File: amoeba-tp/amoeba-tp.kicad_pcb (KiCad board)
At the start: 2 copper layers, 172.5 x 126.6 mm, 153 parts

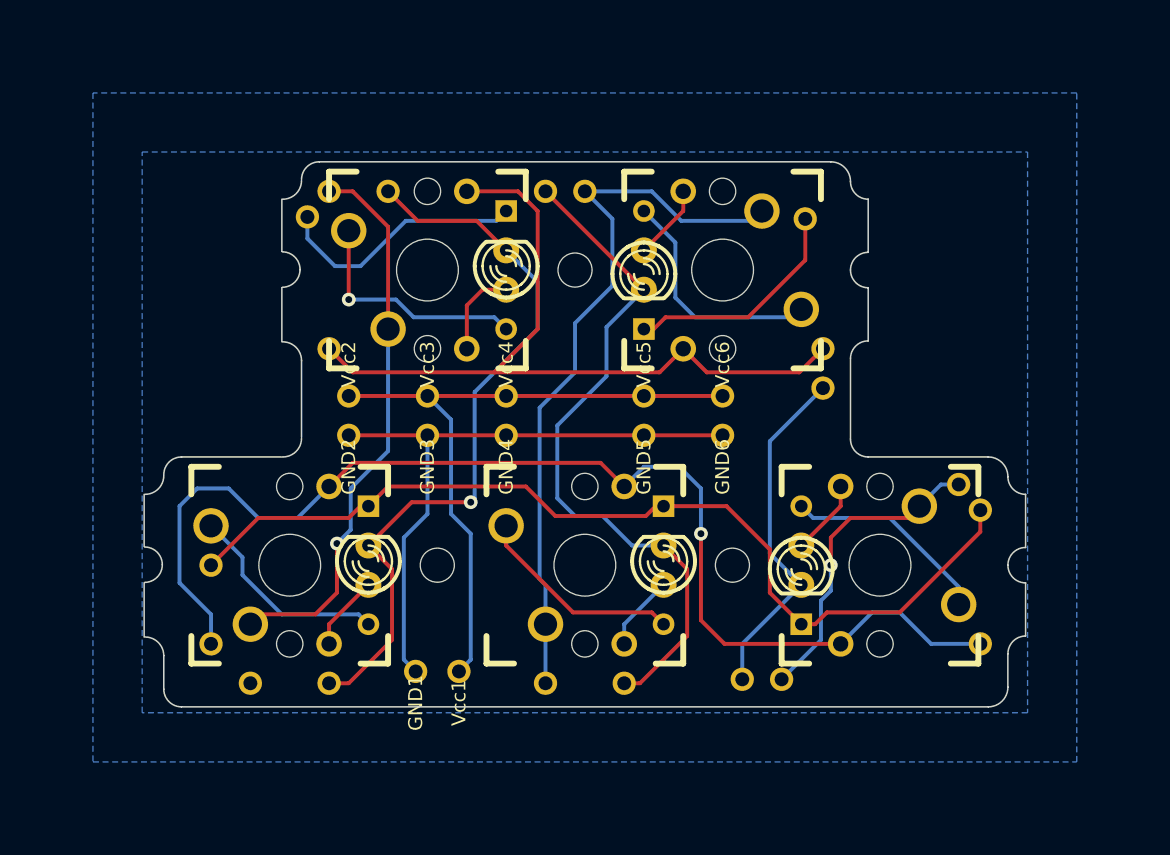
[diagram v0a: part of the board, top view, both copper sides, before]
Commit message: Added fill zones.
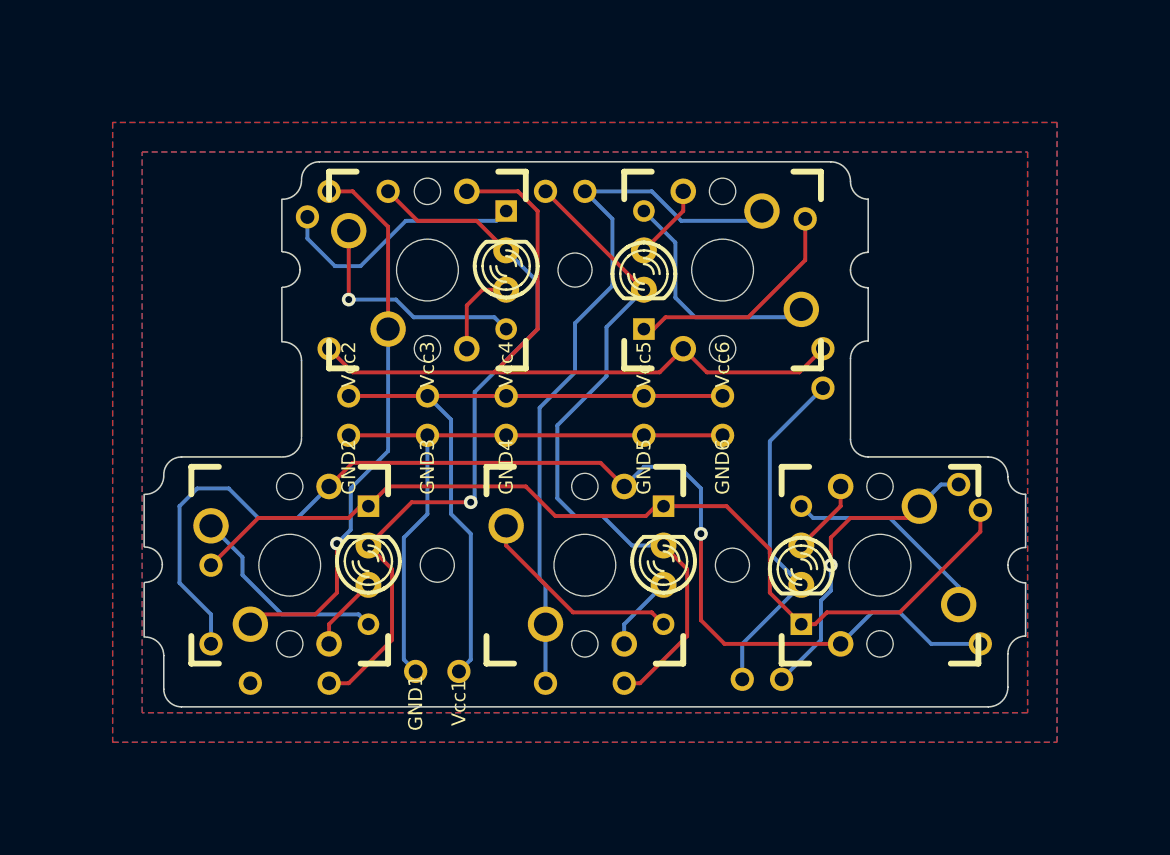
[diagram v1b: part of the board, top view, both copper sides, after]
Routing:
- added copper zone on F.Cu, net N-000007
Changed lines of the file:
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@@
     (links 172)
     (no_connects 40)
-    (area 76.911999 92.024999 172.008001 165.404001)
+    (area 37.184 60.96 220.626 202.846)
     (thickness 1.6)
     (drawings 579)
@@
   (page A3)
   (layers
-    (15 F.Cu signal hide)
+    (15 F.Cu signal)
     (0 B.Cu signal)
     (16 B.Adhes user hide)
@@
     (18 B.Paste user hide)
     (19 F.Paste user hide)
-    (20 B.SilkS user hide)
-    (21 F.SilkS user hide)
+    (20 B.SilkS user)
+    (21 F.SilkS user)
     (22 B.Mask user hide)
     (23 F.Mask user hide)
@@
     (polygon
       (pts
-        (xy 92.71 149.86) (xy 156.21 149.86) (xy 156.21 106.68) (xy 92.71 106.68)
+        (xy 93.98 148.59) (xy 154.94 148.59) (xy 154.94 108.585) (xy 93.98 108.585)
       )
     )
@@
     (polygon
       (pts
-        (xy 95.885 110.49) (xy 95.885 129.54) (xy 95.885 132.08) (xy 96.52 132.08) (xy 97.79 129.54)
-        (xy 104.775 129.54) (xy 105.41 129.54) (xy 106.045 128.905) (xy 106.045 123.825) (xy 104.775 123.19)
-        (xy 104.775 118.745) (xy 105.41 118.745) (xy 105.41 117.475) (xy 104.775 117.475) (xy 104.775 113.03)
-        (xy 105.41 113.03) (xy 106.68 110.49) (xy 104.775 110.49)
+        (xy 106.68 110.49) (xy 105.41 113.03) (xy 104.775 113.03) (xy 104.775 117.475) (xy 105.41 117.475)
+        (xy 105.41 118.745) (xy 104.775 118.745) (xy 104.775 123.19) (xy 106.045 123.825) (xy 106.045 128.905)
+        (xy 105.41 129.54) (xy 97.79 129.54) (xy 96.52 132.08) (xy 95.885 132.08) (xy 95.885 110.49)
+      )
+    )
+  )
+  (zone (net 0) (net_name "") (layer F.Cu) (hatch edge 0.508)
+    (connect_pads (clearance 0.508))
+    (min_thickness 0.254)
+    (keepout (tracks not_allowed) (vias not_allowed) (copperpour not_allowed))
+    (fill (arc_segments 16) (thermal_gap 0.508) (thermal_bridge_width 0.508) (smoothing chamfer))
+    (polygon
+      (pts
+        (xy 163.195 60.96) (xy 164.465 63.5) (xy 165.1 63.5) (xy 165.1 67.945) (xy 164.465 67.945)
+        (xy 164.465 69.215) (xy 165.1 69.215) (xy 165.1 73.66) (xy 163.83 74.295) (xy 163.83 79.375)
+        (xy 164.465 80.01) (xy 172.085 80.01) (xy 173.355 82.55) (xy 173.99 82.55) (xy 173.99 60.96)
+      )
+    )
+  )
+  (zone (net 0) (net_name "") (layer B.Cu) (hatch edge 0.508)
+    (connect_pads (clearance 0.508))
+    (min_thickness 0.254)
+    (keepout (tracks not_allowed) (vias not_allowed) (copperpour not_allowed))
+    (fill (arc_segments 16) (thermal_gap 0.508) (thermal_bridge_width 0.508) (smoothing chamfer))
+    (polygon
+      (pts
+        (xy 140.97 110.49) (xy 142.24 113.03) (xy 142.875 113.03) (xy 142.875 117.475) (xy 142.24 117.475)
+        (xy 142.24 118.745) (xy 142.875 118.745) (xy 142.875 123.19) (xy 141.605 123.825) (xy 141.605 128.905)
+        (xy 142.24 129.54) (xy 151.765 130.175) (xy 152.4 132.08) (xy 153.035 132.08) (xy 153.035 110.49)
+      )
+    )
+  )
+  (zone (net 0) (net_name "") (layer B.Cu) (hatch edge 0.508)
+    (connect_pads (clearance 0.508))
+    (min_thickness 0.254)
+    (keepout (tracks not_allowed) (vias not_allowed) (copperpour not_allowed))
+    (fill (arc_segments 16) (thermal_gap 0.508) (thermal_bridge_width 0.508) (smoothing chamfer))
+    (polygon
+      (pts
+        (xy 153.035 136.525) (xy 152.4 136.525) (xy 152.4 137.795) (xy 153.035 137.795)
+      )
+    )
+  )
+  (zone (net 0) (net_name "") (layer B.Cu) (hatch edge 0.508)
+    (connect_pads (clearance 0.508))
+    (min_thickness 0.254)
+    (keepout (tracks not_allowed) (vias not_allowed) (copperpour not_allowed))
+    (fill (arc_segments 16) (thermal_gap 0.508) (thermal_bridge_width 0.508) (smoothing chamfer))
+    (polygon
+      (pts
+        (xy 153.035 142.24) (xy 152.4 142.24) (xy 152.4 145.415) (xy 151.13 146.685) (xy 153.035 146.685)
+      )
+    )
+  )
+  (zone (net 26) (net_name N-000007) (layer F.Cu) (hatch edge 0.508)
+    (connect_pads (clearance 0.508))
+    (min_thickness 0.254)
+    (fill (arc_segments 16) (thermal_gap 0.508) (thermal_bridge_width 0.508) (smoothing chamfer))
+    (polygon
+      (pts
+        (xy 93.98 148.59) (xy 154.94 148.59) (xy 154.94 108.585) (xy 93.98 108.585)
+      )
+    )
+  )
+  (zone (net 0) (net_name "") (layer F.Cu) (hatch edge 0.508)
+    (priority 1)
+    (connect_pads (clearance 0.508))
+    (min_thickness 0.254)
+    (fill (arc_segments 16) (thermal_gap 0.508) (thermal_bridge_width 0.508) (smoothing chamfer))
+    (polygon
+      (pts
+        (xy 153.035 146.685) (xy 95.885 146.685) (xy 95.885 110.49) (xy 153.035 110.49)
+      )
+    )
+  )
+  (zone (net 0) (net_name "") (layer F.Cu) (hatch edge 0.508)
+    (connect_pads (clearance 0.508))
+    (min_thickness 0.254)
+    (keepout (tracks not_allowed) (vias not_allowed) (copperpour not_allowed))
+    (fill (arc_segments 16) (thermal_gap 0.508) (thermal_bridge_width 0.508) (smoothing chamfer))
+    (polygon
+      (pts
+        (xy 106.68 110.49) (xy 105.41 113.03) (xy 104.775 113.03) (xy 104.775 117.475) (xy 105.41 117.475)
+        (xy 105.41 118.745) (xy 104.775 118.745) (xy 104.775 123.19) (xy 106.045 123.825) (xy 106.045 128.905)
+        (xy 105.41 129.54) (xy 97.79 129.54) (xy 96.52 132.08) (xy 95.885 132.08) (xy 95.885 110.49)
+      )
+    )
+  )
+  (zone (net 0) (net_name "") (layer F.Cu) (hatch edge 0.508)
+    (connect_pads (clearance 0.508))
+    (min_thickness 0.254)
+    (keepout (tracks not_allowed) (vias not_allowed) (copperpour not_allowed))
+    (fill (arc_segments 16) (thermal_gap 0.508) (thermal_bridge_width 0.508) (smoothing chamfer))
+    (polygon
+      (pts
+        (xy 140.97 110.49) (xy 142.24 113.03) (xy 142.875 113.03) (xy 142.875 117.475) (xy 142.24 117.475)
+        (xy 142.24 118.745) (xy 142.875 118.745) (xy 142.875 123.19) (xy 141.605 123.825) (xy 141.605 128.905)
+        (xy 142.24 129.54) (xy 151.765 130.175) (xy 152.4 132.08) (xy 153.035 132.08) (xy 153.035 110.49)
+      )
+    )
+  )
+  (zone (net 0) (net_name "") (layer F.Cu) (hatch edge 0.508)
+    (connect_pads (clearance 0.508))
+    (min_thickness 0.254)
+    (keepout (tracks not_allowed) (vias not_allowed) (copperpour not_allowed))
+    (fill (arc_segments 16) (thermal_gap 0.508) (thermal_bridge_width 0.508) (smoothing chamfer))
+    (polygon
+      (pts
+        (xy 153.035 136.525) (xy 152.4 136.525) (xy 152.4 137.795) (xy 153.035 137.795)
+      )
+    )
+  )
+  (zone (net 0) (net_name "") (layer F.Cu) (hatch edge 0.508)
+    (connect_pads (clearance 0.508))
+    (min_thickness 0.254)
+    (keepout (tracks not_allowed) (vias not_allowed) (copperpour not_allowed))
+    (fill (arc_segments 16) (thermal_gap 0.508) (thermal_bridge_width 0.508) (smoothing chamfer))
+    (polygon
+      (pts
+        (xy 153.035 142.24) (xy 152.4 142.24) (xy 152.4 145.415) (xy 151.13 146.685) (xy 153.035 146.685)
+      )
+    )
+  )
+  (zone (net 0) (net_name "") (layer F.Cu) (hatch edge 0.508)
+    (connect_pads (clearance 0.508))
+    (min_thickness 0.254)
+    (keepout (tracks not_allowed) (vias not_allowed) (copperpour not_allowed))
+    (fill (arc_segments 16) (thermal_gap 0.508) (thermal_bridge_width 0.508) (smoothing chamfer))
+    (polygon
+      (pts
+        (xy 97.79 146.685) (xy 95.885 146.685) (xy 95.885 142.24) (xy 96.52 142.24) (xy 97.155 142.875)
+        (xy 97.155 146.05)
+      )
+    )
+  )
+  (zone (net 0) (net_name "") (layer F.Cu) (hatch edge 0.508)
+    (connect_pads (clearance 0.508))
+    (min_thickness 0.254)
+    (keepout (tracks not_allowed) (vias not_allowed) (copperpour not_allowed))
+    (fill (arc_segments 16) (thermal_gap 0.508) (thermal_bridge_width 0.508) (smoothing chamfer))
+    (polygon
+      (pts
+        (xy 96.52 137.795) (xy 95.885 137.795) (xy 95.885 136.525) (xy 96.52 136.525)
       )
     )

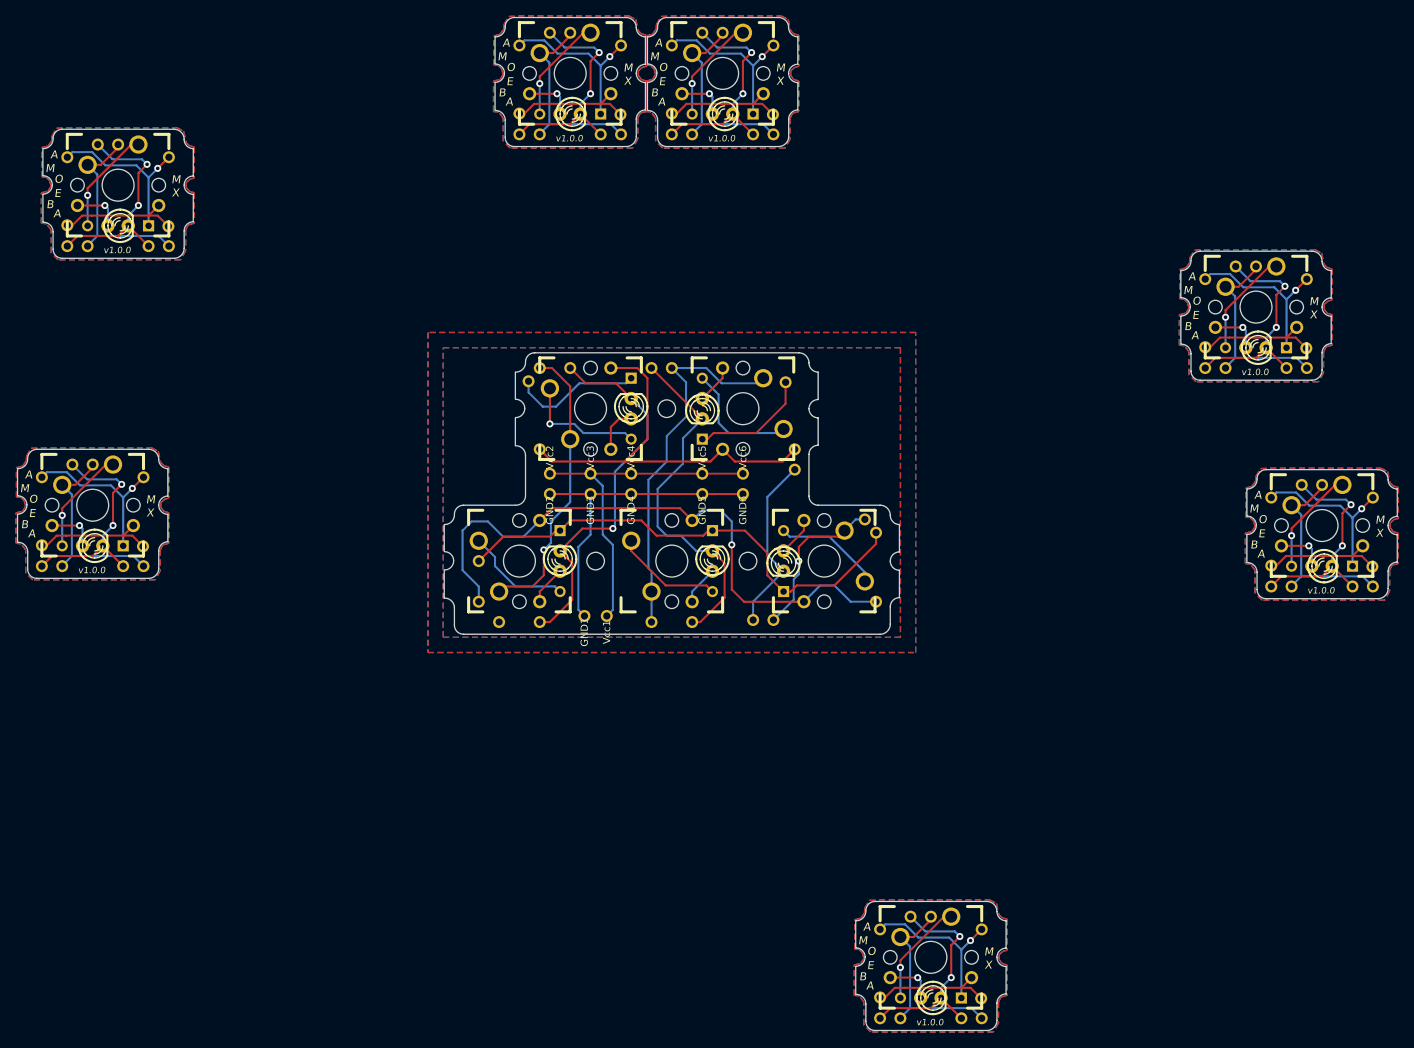
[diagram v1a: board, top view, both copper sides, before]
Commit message: Add labels to PCB and remove Amoeba footprints.
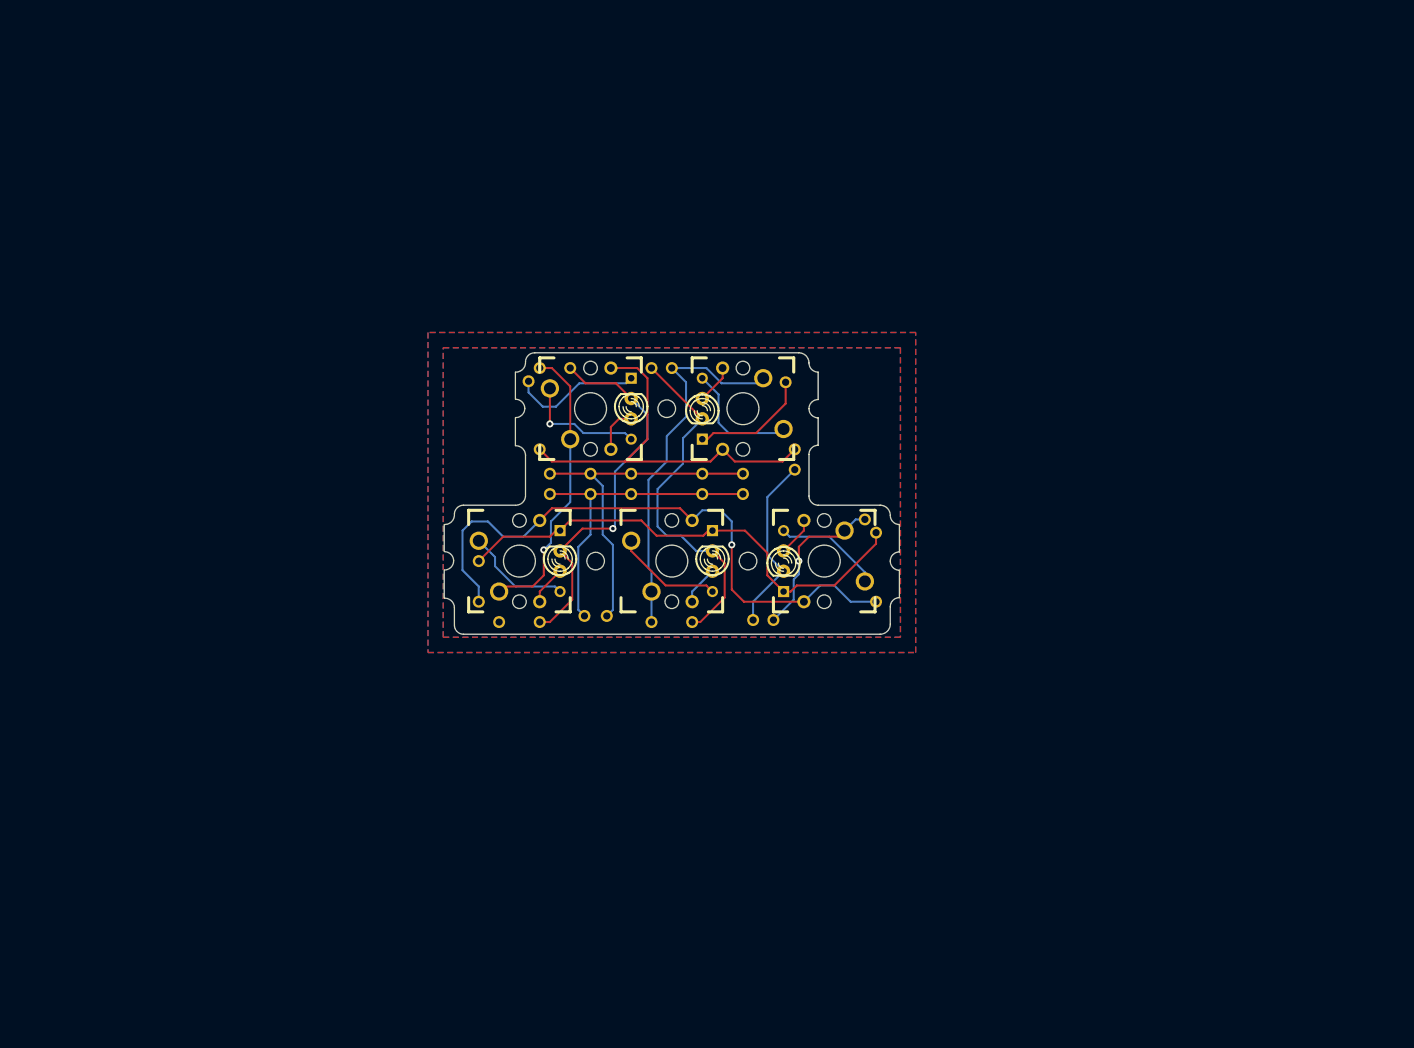
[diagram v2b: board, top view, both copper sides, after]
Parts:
- removed D1 (x7): DIODE, D3
- removed LC (x21), LR (x14), SC (x21), SR (x14): CONN_1, Pad
- removed LED1 (x7): LED, LED-3MM
- removed R1 (x7): RESISTOR, RESISTOR
- removed S1 (x7): MX1A, CHERRY_PCB_100H
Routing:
- net N-000006: track 240.1 -> 43.4 mm, vias 14 -> 0
- net N-000005: track 180.1 -> 0.00 mm
- net N-000001: track 149.5 -> 0.00 mm, vias 7 -> 0
- net N-000004: track 108.4 -> 0.00 mm
- net N-000007: track 133.5 -> 40.3 mm, vias 7 -> 0
- net N-000003: track 42.9 -> 0.00 mm, vias 7 -> 0
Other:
- board size 172.5 x 126.6 mm -> 56.9 x 35.2 mm
- board text added: "G"
- board text added: "GND"
- board text added: "H"
- board text added: "N"
- board text added: "V"
- board text added: "V+"
- board text removed: "A"
- board text removed: "C"
- board text removed: "E"
- board text removed: "M"
- board text removed: "O"
- board text removed: "X"

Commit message: Cleaned up Amoeba TP design.
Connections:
- net /key0:0/LC0 renamed /key:H/LC0
- net /key0:0/LR0 renamed /key:G/LR0
- net /key0:0/SC0 renamed /key:H/SC0
- net /key0:0/SR0 renamed /key:G/SR0
- net /key0:1/LR0 renamed /key:B/LR0
- net /key0:1/SR0 renamed /key:B/SR0
- net /key1:0/LC0 renamed /key:B/LC0
- net /key1:0/SC0 renamed /key:B/SC0
- net /key2:1/LC0 renamed /key:V/LC0
- net /key2:1/SC0 renamed /key:V/SC0
